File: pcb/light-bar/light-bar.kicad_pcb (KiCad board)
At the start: 2 copper layers, 23 parts, among them J1 Conn_01x02

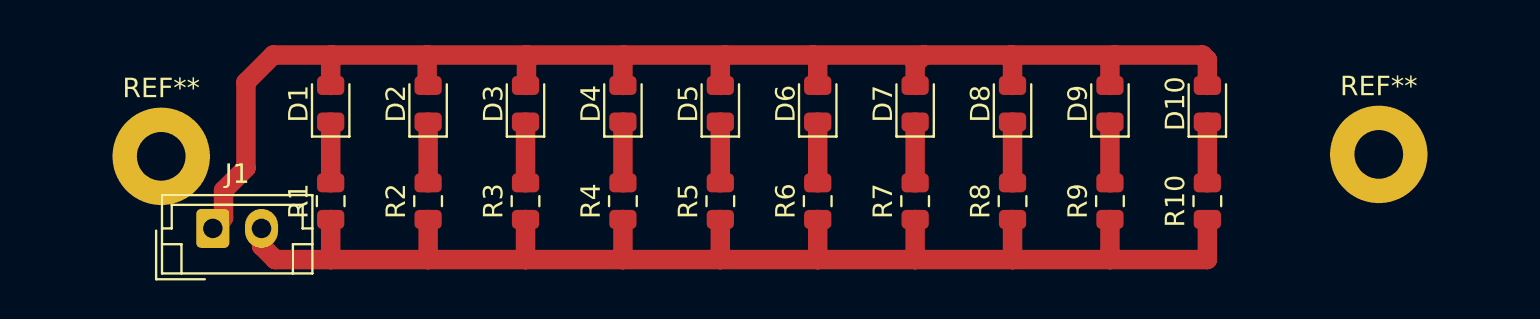
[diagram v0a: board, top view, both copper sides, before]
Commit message: Moved mounting holes
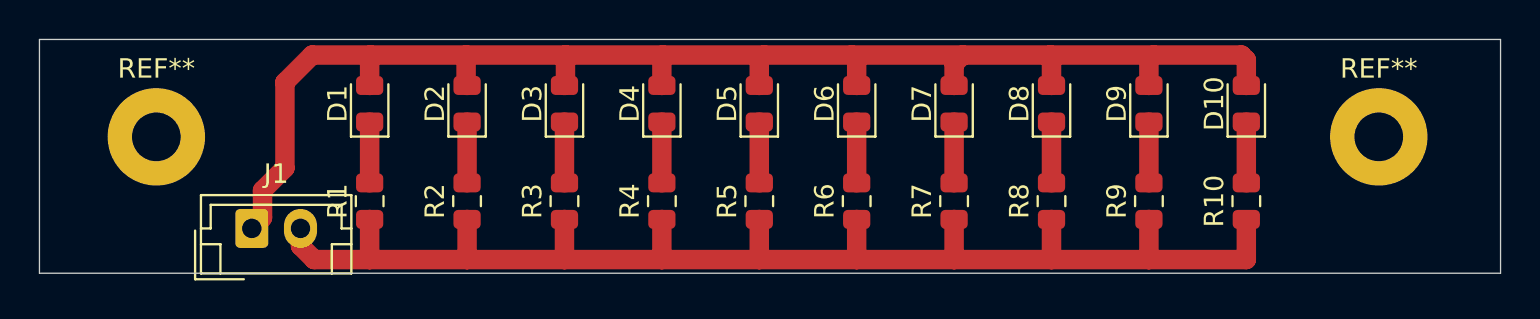
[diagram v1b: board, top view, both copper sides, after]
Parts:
- moved D1 2.00 mm to (117.0, 63.3)
- moved D10 2.00 mm to (161.9, 63.3)
- moved D2 2.00 mm to (122.0, 63.3)
- moved D3 2.00 mm to (127.0, 63.3)
- moved D4 2.00 mm to (131.9, 63.3)
- moved D5 2.00 mm to (136.9, 63.3)
- moved D6 2.00 mm to (141.9, 63.3)
- moved D7 2.00 mm to (146.9, 63.3)
- moved D8 2.00 mm to (151.9, 63.3)
- moved D9 2.00 mm to (156.9, 63.3)
- moved J1 2.00 mm to (110.9, 69.7)
- moved R1 2.00 mm to (117.0, 68.3)
- moved R10 2.00 mm to (161.9, 68.3)
- moved R2 2.00 mm to (122.0, 68.3)
- moved R3 2.00 mm to (127.0, 68.3)
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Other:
- board outline added: 75 x 12 mm
